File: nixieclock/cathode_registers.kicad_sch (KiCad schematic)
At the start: 1 part

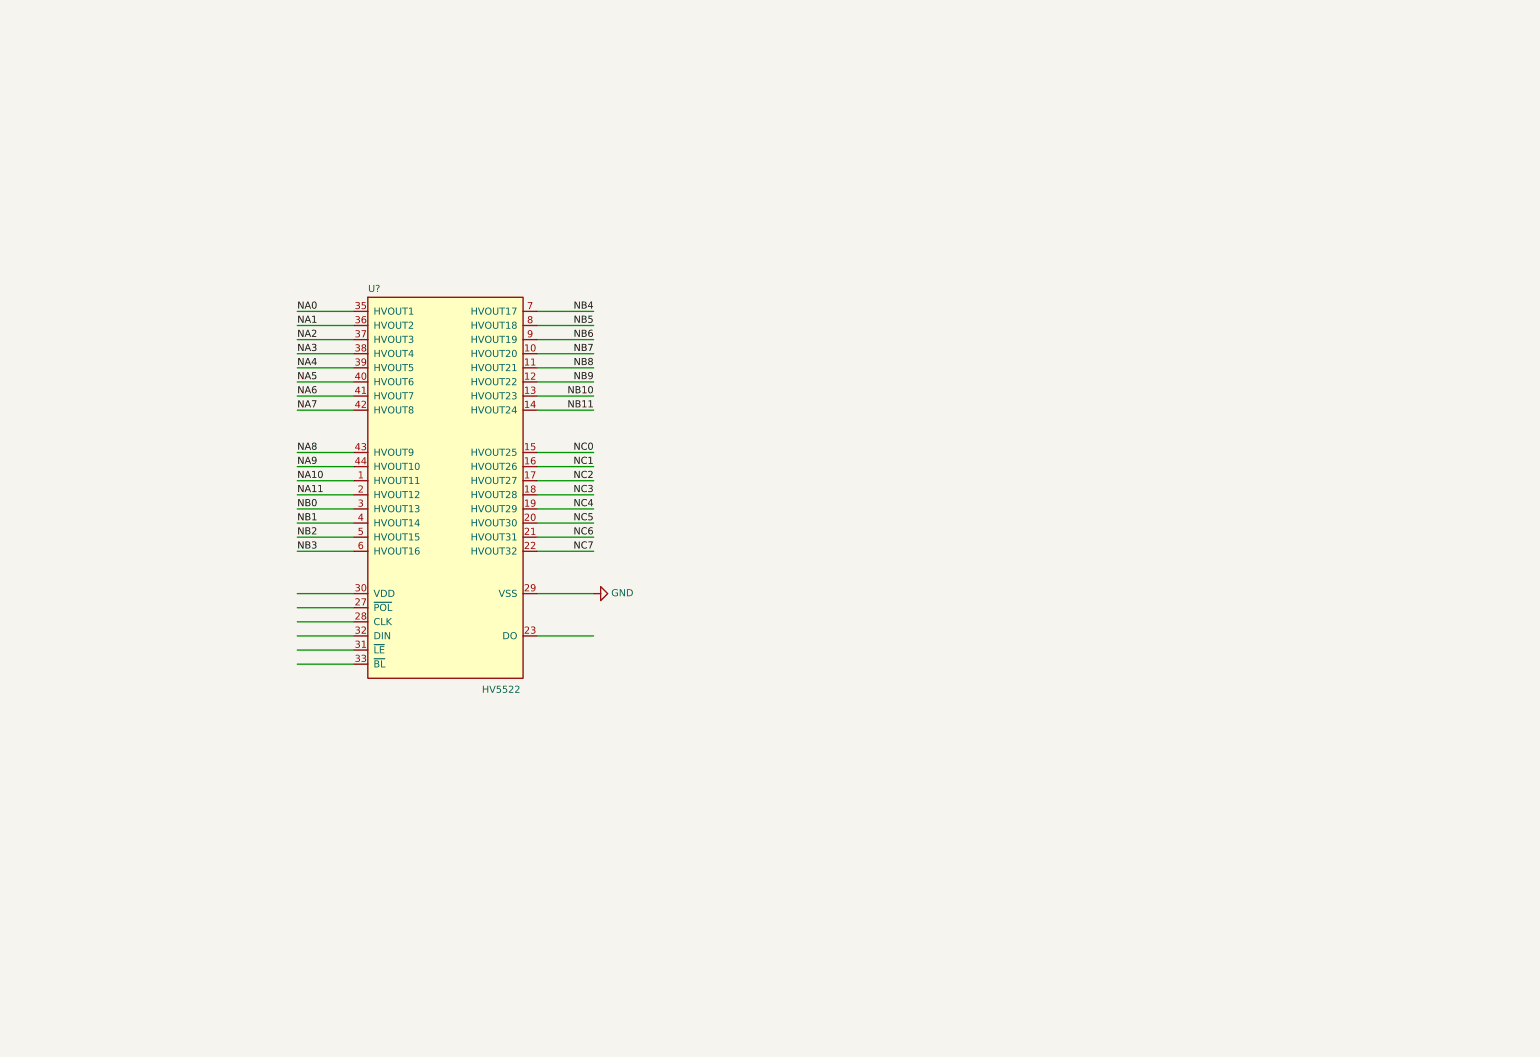
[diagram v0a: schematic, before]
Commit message: finalized power supplies, most footprints, nixie breakout
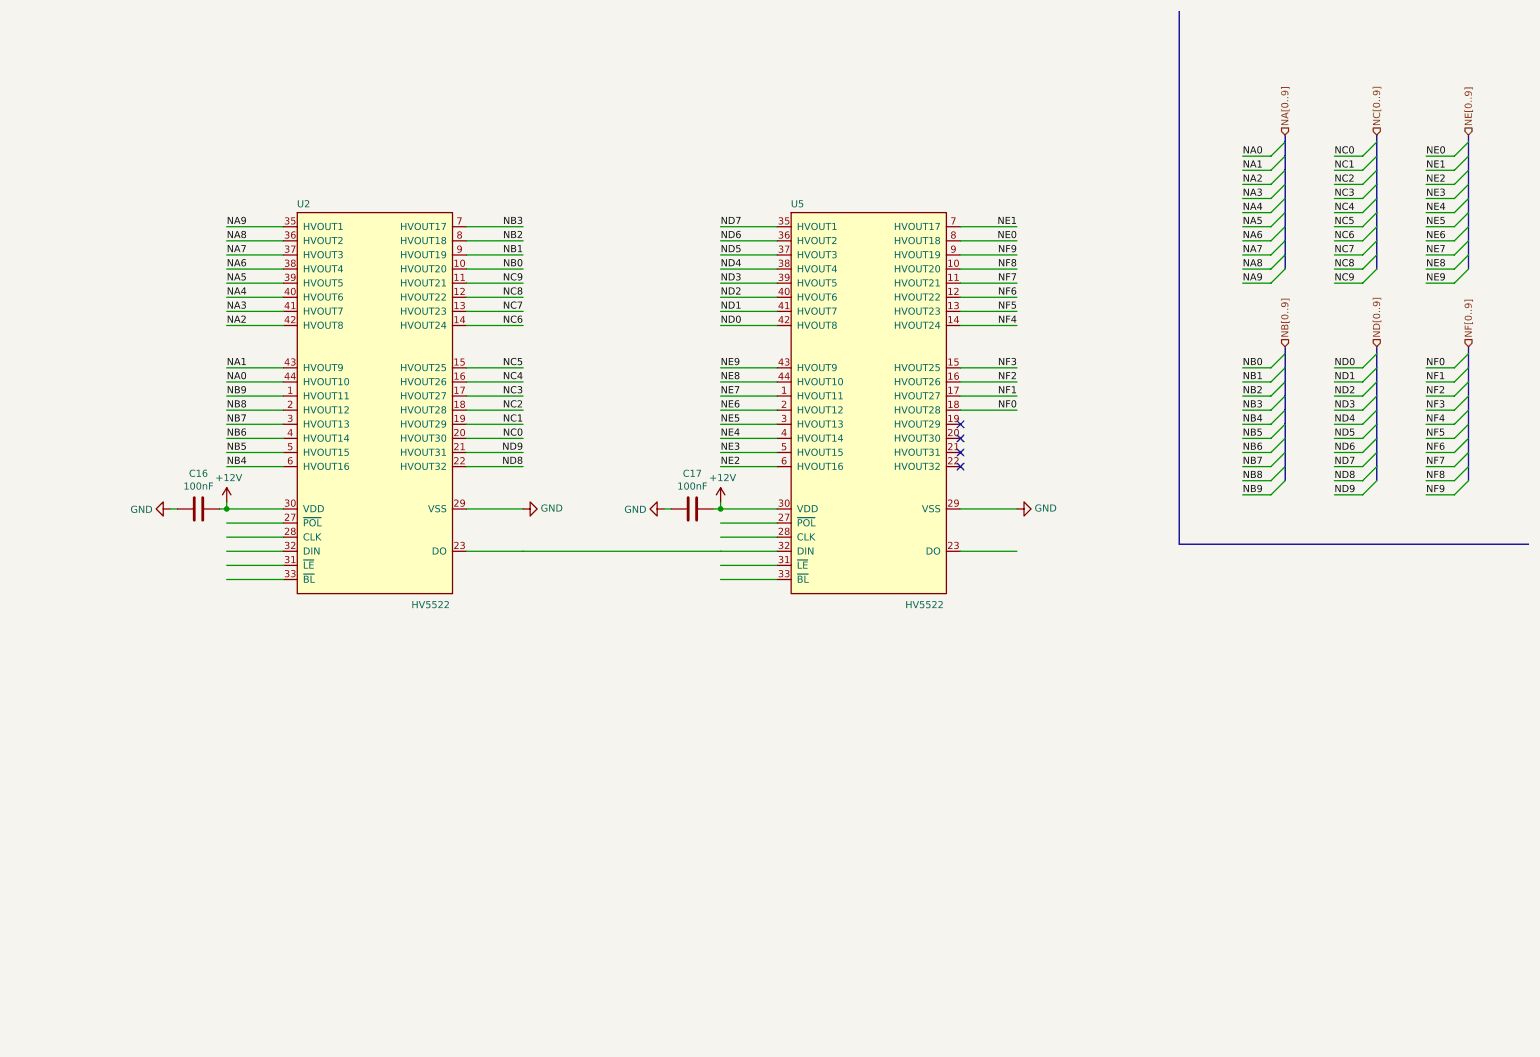
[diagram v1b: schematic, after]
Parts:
- added C16, C17: 100nF, Capacitor_SMD:C_0805_2012Metric_Pad1.15x1.40mm_HandSolder, symbol Device:C
- added U5: HV5522, Package_QFP:PQFP-44_10x10mm_P0.8mm, symbol Personal:HV5522
- U2: renamed from U?; footprint (none) -> Package_QFP:PQFP-44_10x10mm_P0.8mm
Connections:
- net NA10 is gone; now on net NB9: U2.1 (HVOUT11)
- net NA11 is gone; now on net NB8: U2.2 (HVOUT12)
- net NB10 is gone; now on net NC7: U2.13 (HVOUT23)
- net NB11 is gone; now on net NC6: U2.14 (HVOUT24)
- net GND: now also C16.2, C17.2, U5.29 (VSS)
- net NA0: now also U2.44 (HVOUT10); no longer U2.35 (HVOUT1)
- net NA1: now also U2.43 (HVOUT9); no longer U2.36 (HVOUT2)
- net NA2: now also U2.42 (HVOUT8); no longer U2.37 (HVOUT3)
- net NA3: now also U2.41 (HVOUT7); no longer U2.38 (HVOUT4)
- net NA4: now also U2.40 (HVOUT6); no longer U2.39 (HVOUT5)
- net NA5: now also U2.39 (HVOUT5); no longer U2.40 (HVOUT6)
- net NA6: now also U2.38 (HVOUT4); no longer U2.41 (HVOUT7)
- net NA7: now also U2.37 (HVOUT3); no longer U2.42 (HVOUT8)
- net NA8: now also U2.36 (HVOUT2); no longer U2.43 (HVOUT9)
- net NA9: now also U2.35 (HVOUT1); no longer U2.44 (HVOUT10)
- net NB0: now also U2.10 (HVOUT20); no longer U2.3 (HVOUT13)
- net NB1: now also U2.9 (HVOUT19); no longer U2.4 (HVOUT14)
- net NB2: now also U2.8 (HVOUT18); no longer U2.5 (HVOUT15)
- net NB3: now also U2.7 (HVOUT17); no longer U2.6 (HVOUT16)
- net NB4: now also U2.6 (HVOUT16); no longer U2.7 (HVOUT17)
- net NB5: now also U2.5 (HVOUT15); no longer U2.8 (HVOUT18)
- net NB6: now also U2.4 (HVOUT14); no longer U2.9 (HVOUT19)
- net NB7: now also U2.3 (HVOUT13); no longer U2.10 (HVOUT20)
- net NB8: no longer U2.11 (HVOUT21)
- net NB9: no longer U2.12 (HVOUT22)
- net NC0: now also U2.20 (HVOUT30); no longer U2.15 (HVOUT25)
- net NC1: now also U2.19 (HVOUT29); no longer U2.16 (HVOUT26)
- net NC2: now also U2.18 (HVOUT28); no longer U2.17 (HVOUT27)
- net NC3: now also U2.17 (HVOUT27); no longer U2.18 (HVOUT28)
- net NC4: now also U2.16 (HVOUT26); no longer U2.19 (HVOUT29)
- net NC5: now also U2.15 (HVOUT25); no longer U2.20 (HVOUT30)
- net NC6: no longer U2.21 (HVOUT31)
- net NC7: no longer U2.22 (HVOUT32)
- net at U2.23 (DO): now also U5.32 (DIN)
- net +12V: now reaches U2.30 (VDD)
- net +12V: now also C16.1, C17.1, U5.30 (VDD)
- new net NC8: U2.12 (HVOUT22)
- new net NC9: U2.11 (HVOUT21)
- new net ND0: U5.42 (HVOUT8)
- new net ND1: U5.41 (HVOUT7)
- new net ND2: U5.40 (HVOUT6)
- new net ND3: U5.39 (HVOUT5)
- new net ND4: U5.38 (HVOUT4)
- new net ND5: U5.37 (HVOUT3)
- new net ND6: U5.36 (HVOUT2)
- new net ND7: U5.35 (HVOUT1)
- new net ND8: U2.22 (HVOUT32)
- new net ND9: U2.21 (HVOUT31)
- new net NE0: U5.8 (HVOUT18)
- new net NE1: U5.7 (HVOUT17)
- new net NE2: U5.6 (HVOUT16)
- new net NE3: U5.5 (HVOUT15)
- new net NE4: U5.4 (HVOUT14)
- new net NE5: U5.3 (HVOUT13)
- new net NE6: U5.2 (HVOUT12)
- new net NE7: U5.1 (HVOUT11)
- new net NE8: U5.44 (HVOUT10)
- new net NE9: U5.43 (HVOUT9)
- new net NF0: U5.18 (HVOUT28)
- new net NF1: U5.17 (HVOUT27)
- new net NF2: U5.16 (HVOUT26)
- new net NF3: U5.15 (HVOUT25)
- new net NF4: U5.14 (HVOUT24)
- new net NF5: U5.13 (HVOUT23)
- new net NF6: U5.12 (HVOUT22)
- new net NF7: U5.11 (HVOUT21)
- new net NF8: U5.10 (HVOUT20)
- new net NF9: U5.9 (HVOUT19)
- no-connect marks 0 -> 4
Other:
- moved on the sheet: U2

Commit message: added neon bulbs, finalized cathode registers
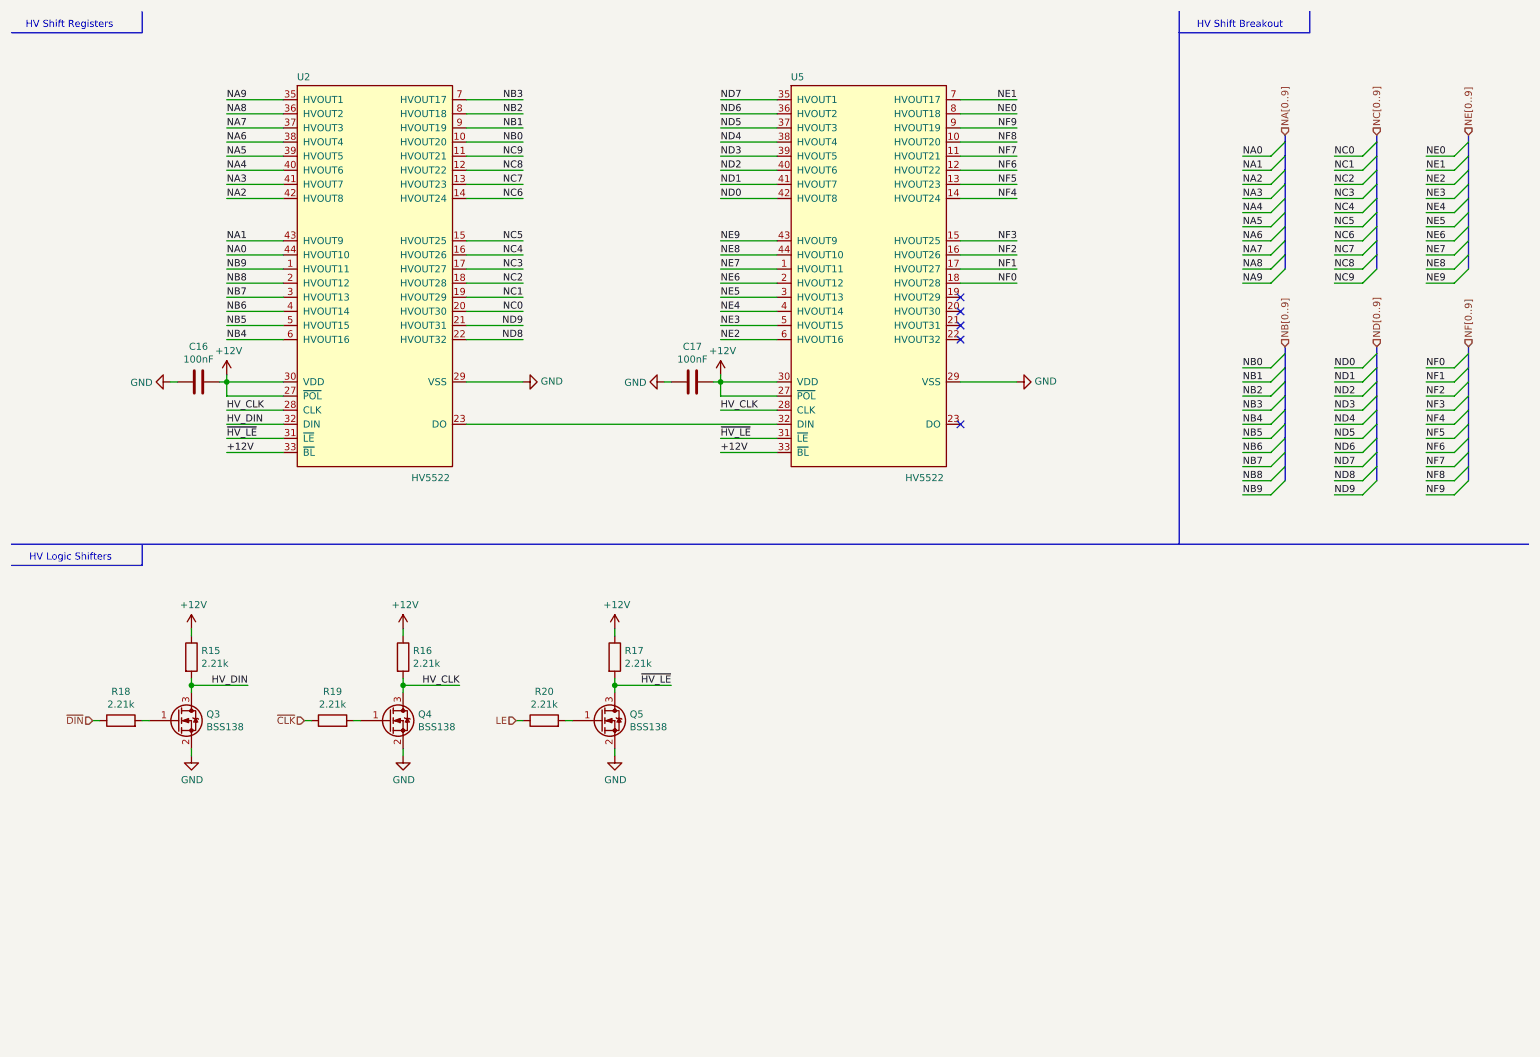
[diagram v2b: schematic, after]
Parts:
- added Q3, Q4, Q5: BSS138, Package_TO_SOT_SMD:SOT-23, symbol Transistor_FET:BSS138
- added R15, R16, R17, R18, R19, R20: 2.21k, Resistor_SMD:R_0805_2012Metric_Pad1.15x1.40mm_HandSolder, symbol Device:R
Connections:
- net +12V: now also U2.27 (~POL), U2.33 (~BL), U5.27 (~POL), U5.33 (~BL), R15.1, R16.1, R17.1
- net GND: now also Q3.2 (S), Q4.2 (S), Q5.2 (S)
- net HV_CLK: now reaches U5.28 (CLK)
- net HV_CLK: now also U2.28 (CLK), Q4.3 (D), R16.2
- net ~HV_LE: now reaches U5.31 (~LE)
- net ~HV_LE: now also U2.31 (~LE), Q5.3 (D), R17.2
- net HV_DIN: now reaches U2.32 (DIN)
- net HV_DIN: now also Q3.3 (D), R15.2
- new net: Q5.1 (G), R20.2
- new net: Q3.1 (G), R18.2
- new net: Q4.1 (G), R19.2
- new net LE: R20.1
- new net ~CLK: R19.1
- new net ~DIN: R18.1
- no-connect marks 4 -> 5
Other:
- note added: "HV Logic Shifters"
- note added: "HV Shift Breakout"
- note added: "HV Shift Registers"
- moved on the sheet: C16, C17, U2, U5

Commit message: began routing PCB, finalized registers design
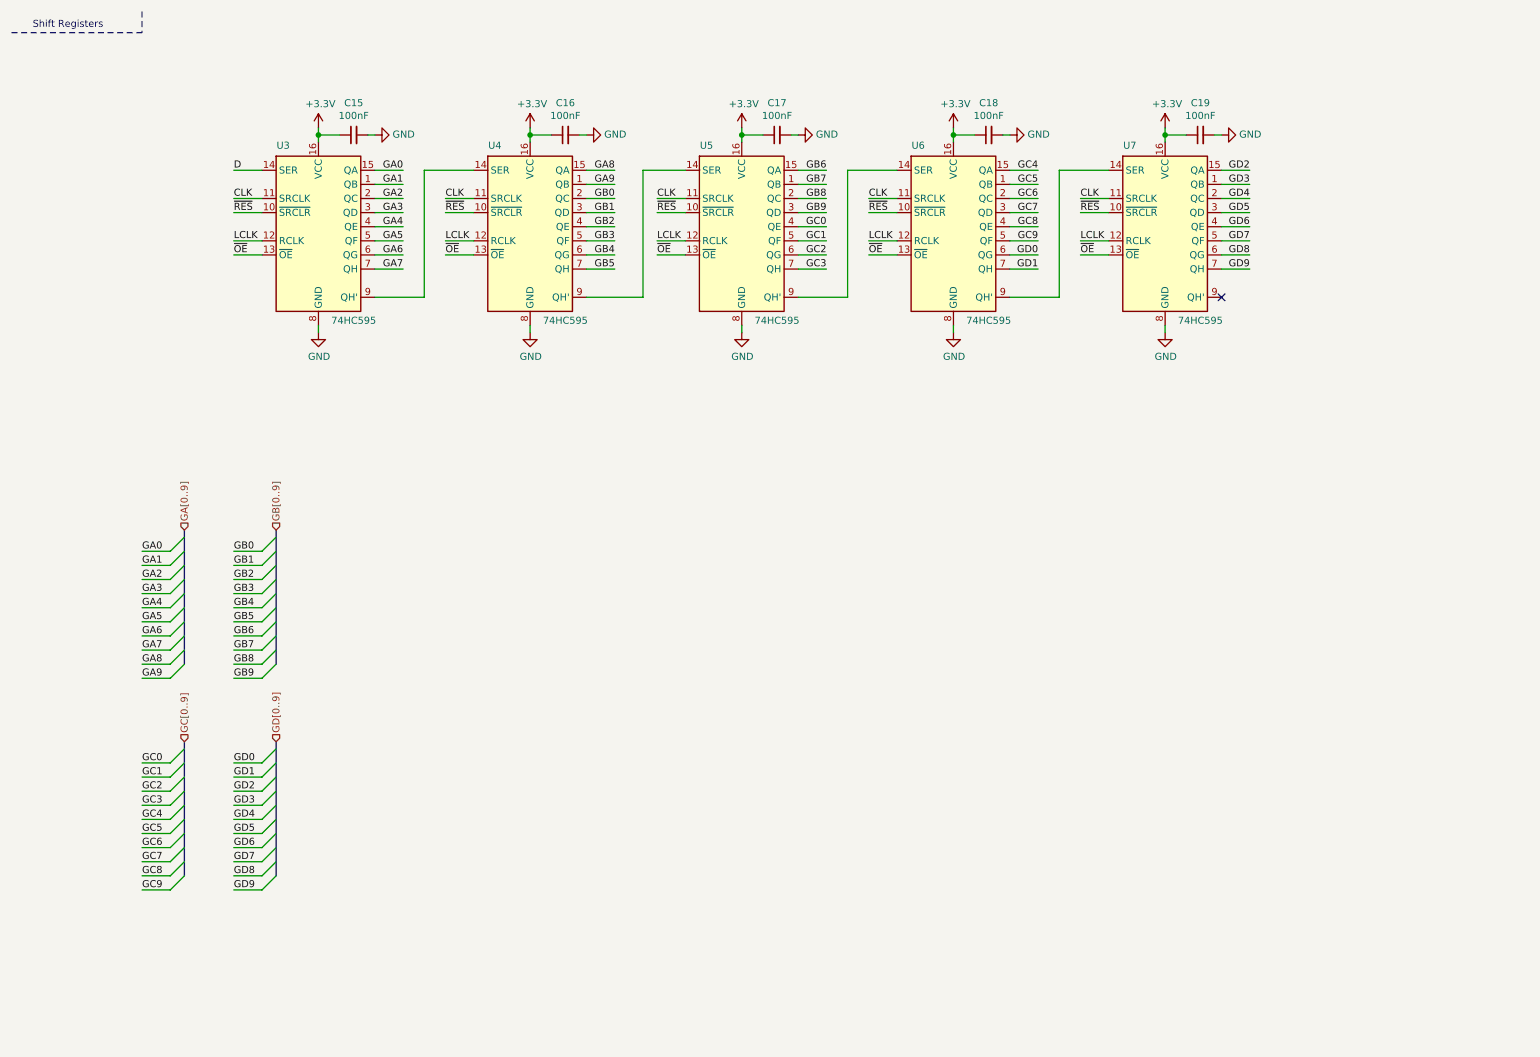
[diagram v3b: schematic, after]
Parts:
- removed C16, C17: 100nF, Capacitor_SMD:C_0805_2012Metric_Pad1.15x1.40mm_HandSolder, symbol Device:C
- removed Q3, Q4, Q5: BSS138, Package_TO_SOT_SMD:SOT-23, symbol Transistor_FET:BSS138
- removed R15, R16, R17, R18, R19, R20: 2.21k, Resistor_SMD:R_0805_2012Metric_Pad1.15x1.40mm_HandSolder, symbol Device:R
- removed U2, U5: HV5522, Package_QFP:PQFP-44_10x10mm_P0.8mm, symbol Personal:HV5522
- added C15, C16, C17, C18, C19: 100nF, Capacitor_SMD:C_0805_2012Metric_Pad1.15x1.40mm_HandSolder, symbol Device:C_Small
- added U3, U4, U5, U6, U7: 74HC595, Package_SO:SOIC-16_4.55x10.3mm_P1.27mm, symbol 74xx:74HC595
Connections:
- net GND: now also C15.2, C16.2, C17.2, C18.2, C19.2, U3.8 (GND), U4.8 (GND), U5.8 (GND), U6.8 (GND), U7.8 (GND)
- new net: U3.9 (QH'), U4.14 (SER)
- new net: U4.9 (QH'), U5.14 (SER)
- new net: U5.9 (QH'), U6.14 (SER)
- new net: U6.9 (QH'), U7.14 (SER)
- new net +3V3: C15.1, C16.1, C17.1, C18.1, C19.1, U3.16 (VCC), U4.16 (VCC), U5.16 (VCC), U6.16 (VCC), U7.16 (VCC)
- new net CLK: U3.11 (SRCLK), U4.11 (SRCLK), U5.11 (SRCLK), U6.11 (SRCLK), U7.11 (SRCLK)
- new net D: U3.14 (SER)
- new net GA0: U3.15 (QA)
- new net GA1: U3.1 (QB)
- new net GA2: U3.2 (QC)
- new net GA3: U3.3 (QD)
- new net GA4: U3.4 (QE)
- new net GA5: U3.5 (QF)
- new net GA6: U3.6 (QG)
- new net GA7: U3.7 (QH)
- new net GA8: U4.15 (QA)
- new net GA9: U4.1 (QB)
- new net GB0: U4.2 (QC)
- new net GB1: U4.3 (QD)
- new net GB2: U4.4 (QE)
- new net GB3: U4.5 (QF)
- new net GB4: U4.6 (QG)
- new net GB5: U4.7 (QH)
- new net GB6: U5.15 (QA)
- new net GB7: U5.1 (QB)
- new net GB8: U5.2 (QC)
- new net GB9: U5.3 (QD)
- new net GC0: U5.4 (QE)
- new net GC1: U5.5 (QF)
- new net GC2: U5.6 (QG)
- new net GC3: U5.7 (QH)
- new net GC4: U6.15 (QA)
- new net GC5: U6.1 (QB)
- new net GC6: U6.2 (QC)
- new net GC7: U6.3 (QD)
- new net GC8: U6.4 (QE)
- new net GC9: U6.5 (QF)
- new net GD0: U6.6 (QG)
- new net GD1: U6.7 (QH)
- new net GD2: U7.15 (QA)
- new net GD3: U7.1 (QB)
- new net GD4: U7.2 (QC)
- new net GD5: U7.3 (QD)
- new net GD6: U7.4 (QE)
- new net GD7: U7.5 (QF)
- new net GD8: U7.6 (QG)
- new net GD9: U7.7 (QH)
- new net LCLK: U3.12 (RCLK), U4.12 (RCLK), U5.12 (RCLK), U6.12 (RCLK), U7.12 (RCLK)
- new net ~OE: U3.13 (~OE), U4.13 (~OE), U5.13 (~OE), U6.13 (~OE), U7.13 (~OE)
- new net ~RES: U3.10 (~SRCLR), U4.10 (~SRCLR), U5.10 (~SRCLR), U6.10 (~SRCLR), U7.10 (~SRCLR)
- no-connect marks 5 -> 1
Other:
- note added: "Shift Registers"
- note removed: "HV Logic Shifters"
- note removed: "HV Shift Breakout"
- note removed: "HV Shift Registers"
- company: Bastian de Byl -> (none)

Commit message: mostly finalized pcb layout, silkscreen graphics, etc
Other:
- note added: "Breakout"
- company: (none) -> Bastian de Byl

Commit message: finalized design, fixed USB C receptacle for hand soldering
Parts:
- C15, C16, C17, C18, C19: footprint Capacitor_SMD:C_0805_2012Metric_Pad1.15x1.40mm_HandSolder -> Capacitor_SMD:C_0603_1608Metric_Pad1.05x0.95mm_HandSolder
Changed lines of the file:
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@@
     (property "Reference" "C15" (id 0) (at 73.66 28.5177 90))
     (property "Value" "100nF" (id 1) (at 73.66 30.816 90))
-    (property "Footprint" "Capacitor_SMD:C_0805_2012Metric_Pad1.15x1.40mm_HandSolder" (id 2) (at 73.66 34.29 0)
+    (property "Footprint" "Capacitor_SMD:C_0603_1608Metric_Pad1.05x0.95mm_HandSolder" (id 2) (at 73.66 34.29 0)
       (effects (font (size 1.27 1.27)) hide)
     )
@@
     (property "Reference" "C16" (id 0) (at 111.76 28.5177 90))
     (property "Value" "100nF" (id 1) (at 111.76 30.816 90))
-    (property "Footprint" "Capacitor_SMD:C_0805_2012Metric_Pad1.15x1.40mm_HandSolder" (id 2) (at 111.76 34.29 0)
+    (property "Footprint" "Capacitor_SMD:C_0603_1608Metric_Pad1.05x0.95mm_HandSolder" (id 2) (at 111.76 34.29 0)
       (effects (font (size 1.27 1.27)) hide)
     )
@@
     (property "Reference" "C17" (id 0) (at 149.86 28.5177 90))
     (property "Value" "100nF" (id 1) (at 149.86 30.816 90))
-    (property "Footprint" "Capacitor_SMD:C_0805_2012Metric_Pad1.15x1.40mm_HandSolder" (id 2) (at 149.86 34.29 0)
+    (property "Footprint" "Capacitor_SMD:C_0603_1608Metric_Pad1.05x0.95mm_HandSolder" (id 2) (at 149.86 34.29 0)
       (effects (font (size 1.27 1.27)) hide)
     )
@@
     (property "Reference" "C18" (id 0) (at 187.96 28.5177 90))
     (property "Value" "100nF" (id 1) (at 187.96 30.816 90))
-    (property "Footprint" "Capacitor_SMD:C_0805_2012Metric_Pad1.15x1.40mm_HandSolder" (id 2) (at 187.96 34.29 0)
+    (property "Footprint" "Capacitor_SMD:C_0603_1608Metric_Pad1.05x0.95mm_HandSolder" (id 2) (at 187.96 34.29 0)
       (effects (font (size 1.27 1.27)) hide)
     )
@@
     (property "Reference" "C19" (id 0) (at 226.06 28.5177 90))
     (property "Value" "100nF" (id 1) (at 226.06 30.816 90))
-    (property "Footprint" "Capacitor_SMD:C_0805_2012Metric_Pad1.15x1.40mm_HandSolder" (id 2) (at 226.06 34.29 0)
+    (property "Footprint" "Capacitor_SMD:C_0603_1608Metric_Pad1.05x0.95mm_HandSolder" (id 2) (at 226.06 34.29 0)
       (effects (font (size 1.27 1.27)) hide)
     )
